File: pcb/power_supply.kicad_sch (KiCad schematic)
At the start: 39 parts, among them J101 TO_IO, U101 10M02SCE144, U102 74LVC2G17, U103 74LVC2G17, U104 74LVC2G17, U105 74LVC2G17

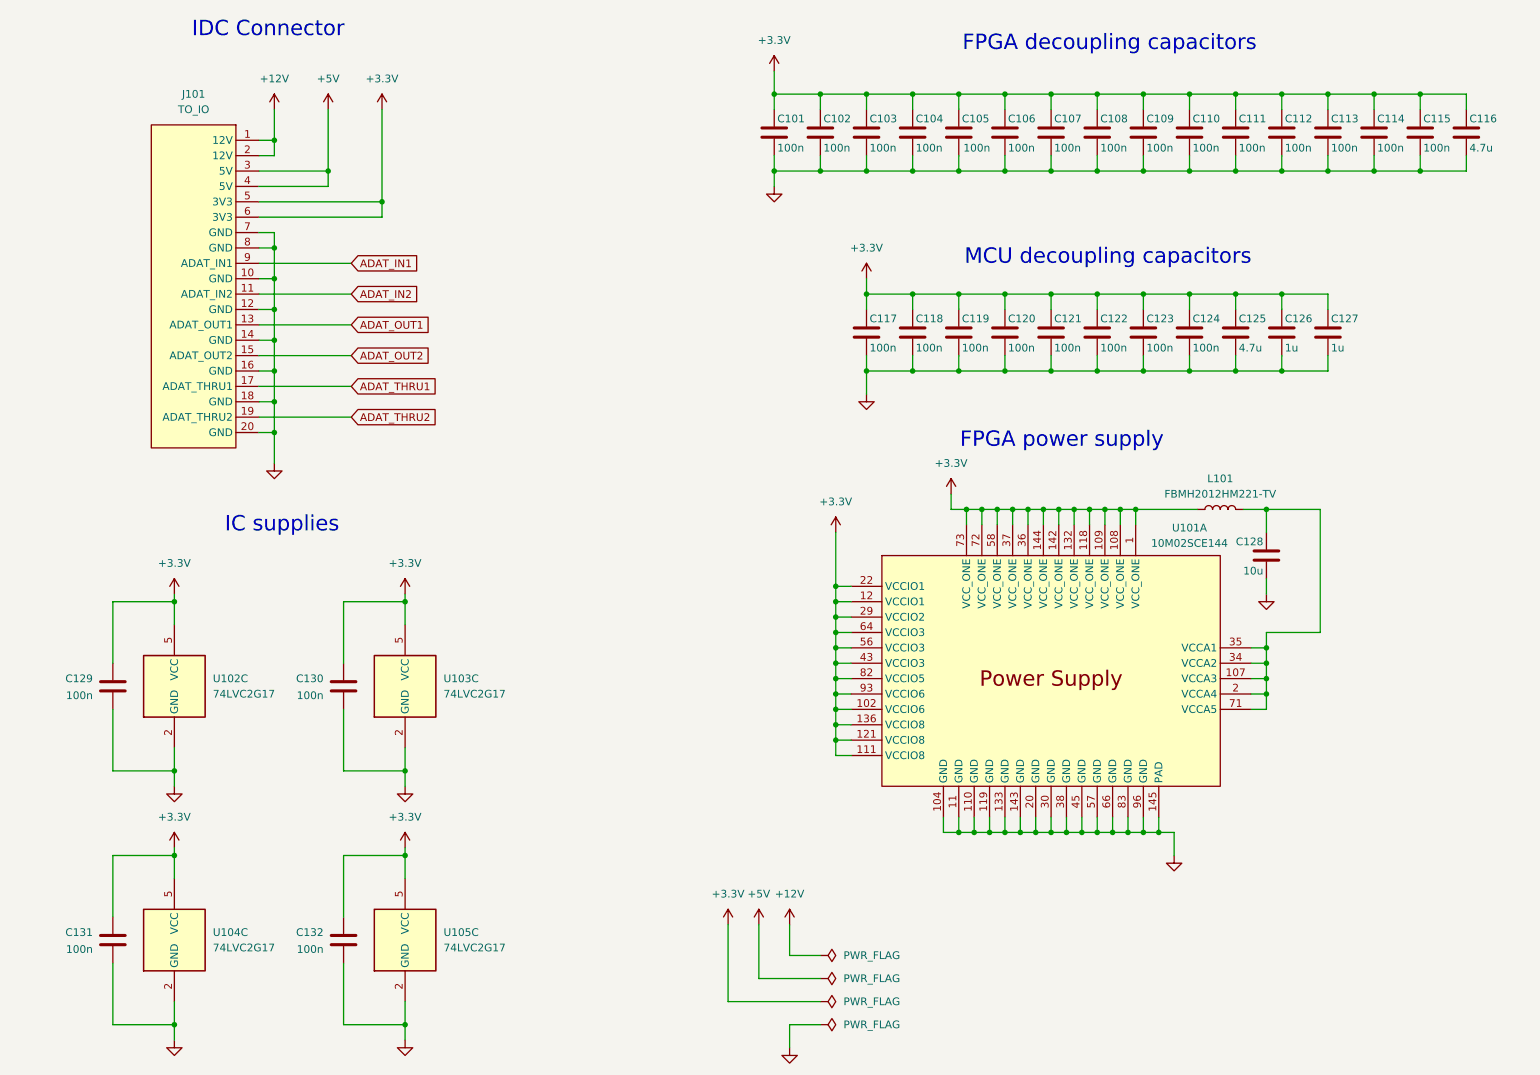
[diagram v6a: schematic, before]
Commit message: Start routing main board
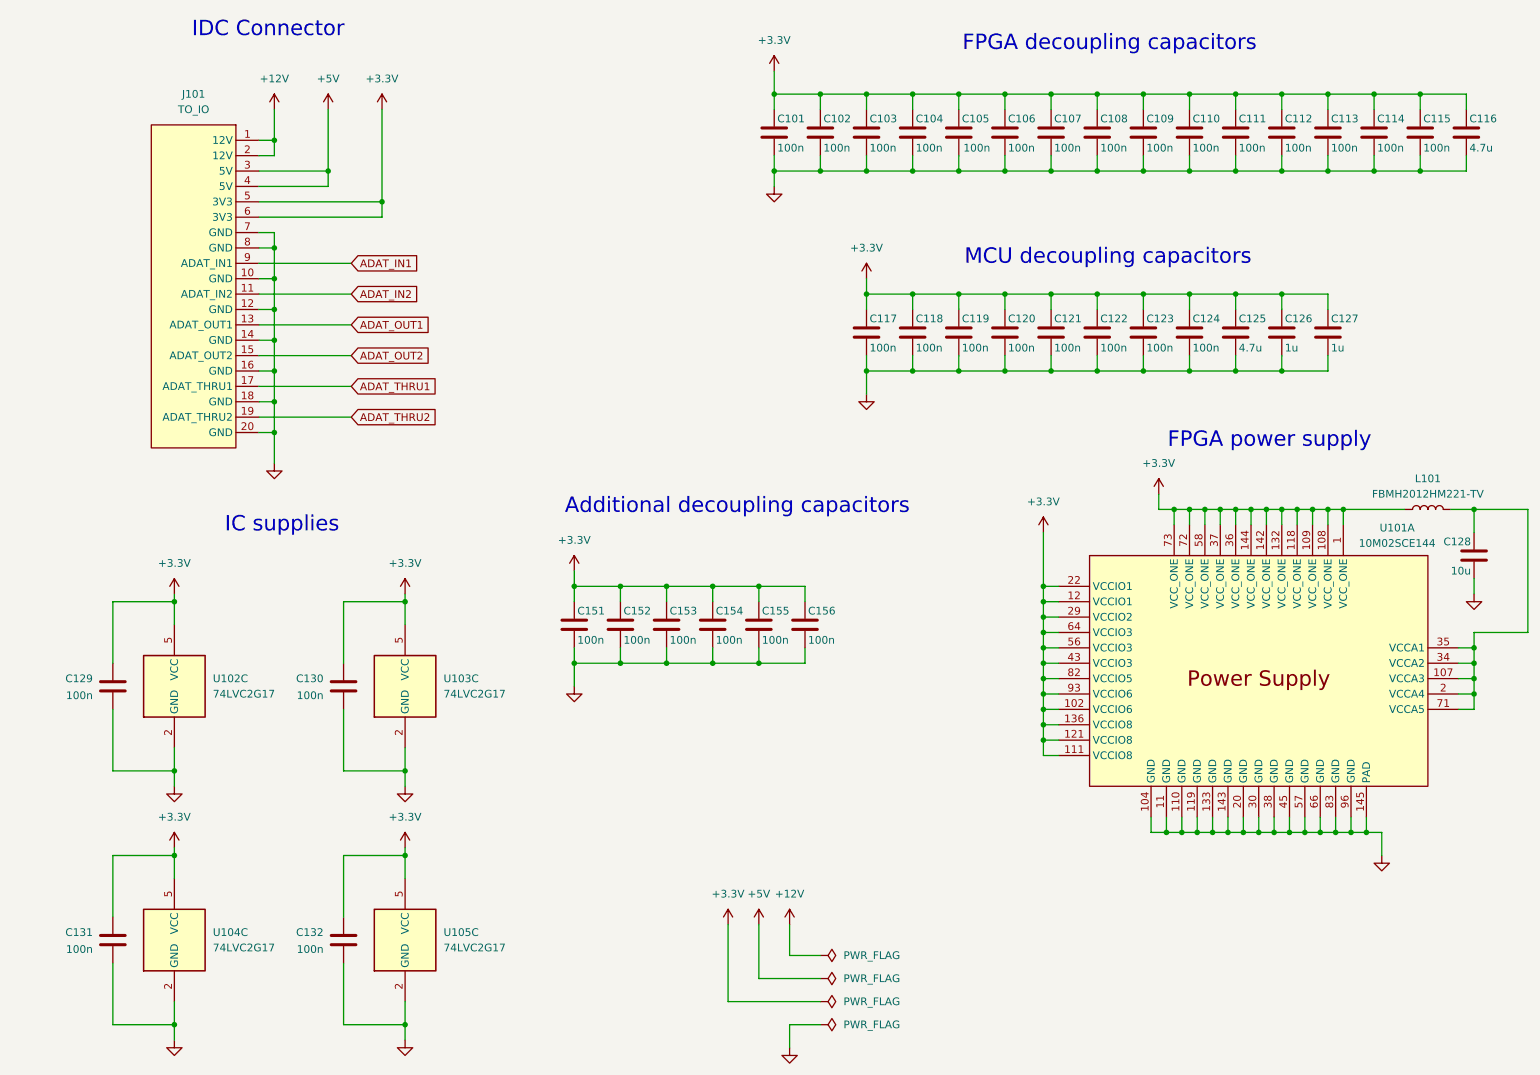
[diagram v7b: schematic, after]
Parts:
- added C151, C152, C153, C154, C155, C156: 100n, Capacitor_SMD:C_0805_2012Metric_Pad1.18x1.45mm_HandSolder, symbol Device:C
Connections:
- net +3.3V: now also C151.1, C152.1, C153.1, C154.1, C155.1, C156.1
- net GND: now also C151.2, C152.2, C153.2, C154.2, C155.2, C156.2
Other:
- note added: "Additional decoupling capacitors"
- moved on the sheet: C128, L101, U101A

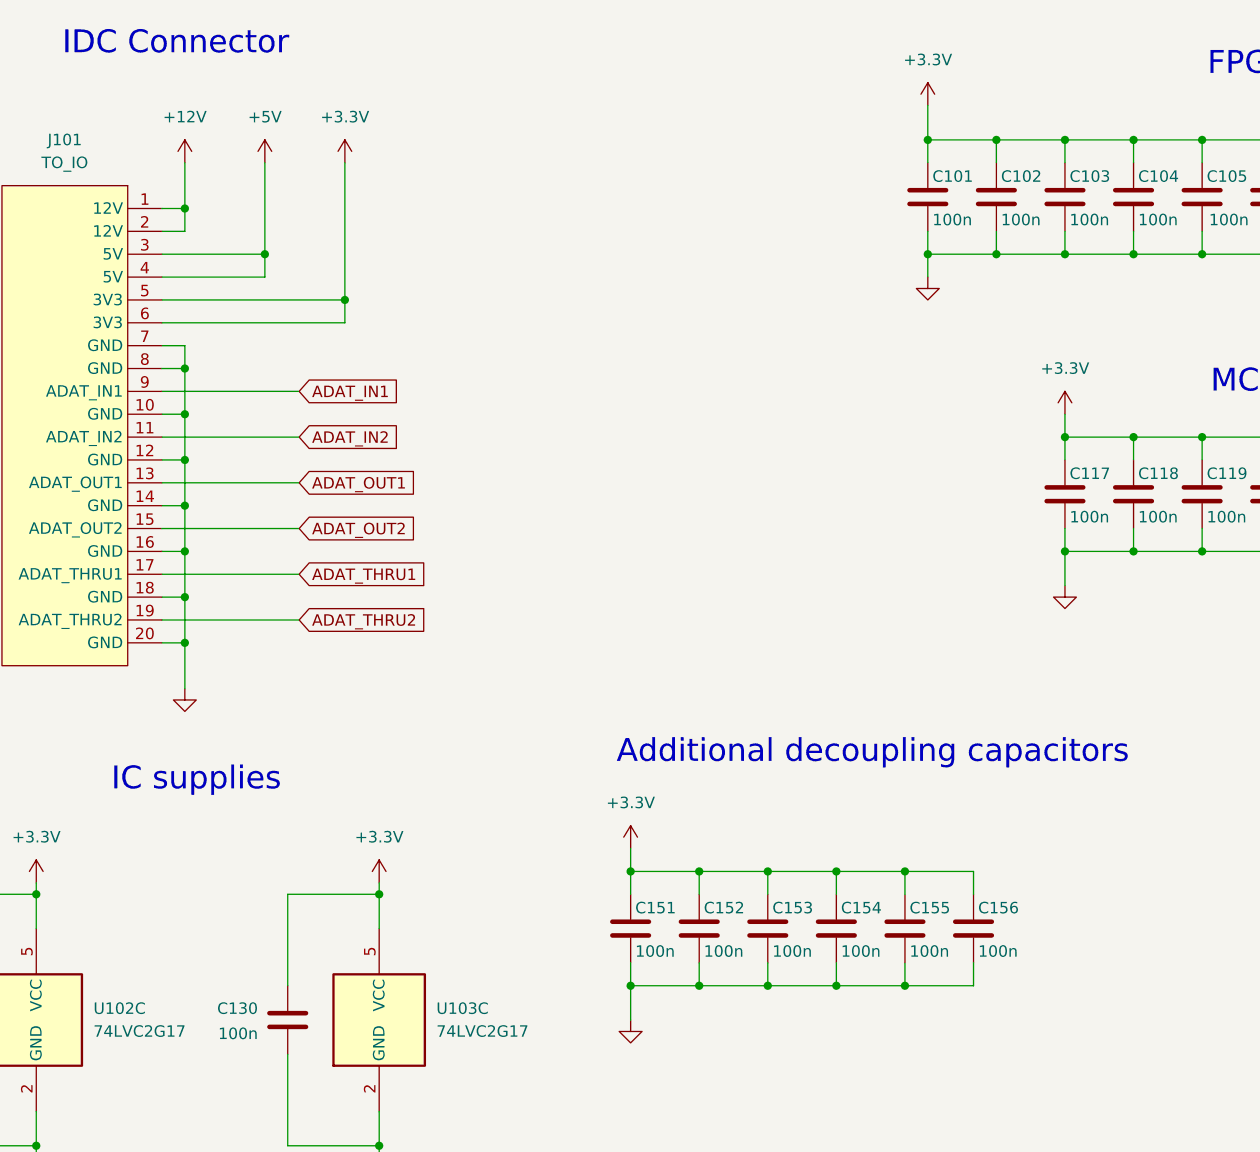
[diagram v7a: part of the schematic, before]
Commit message: Finish first revision of main pcb
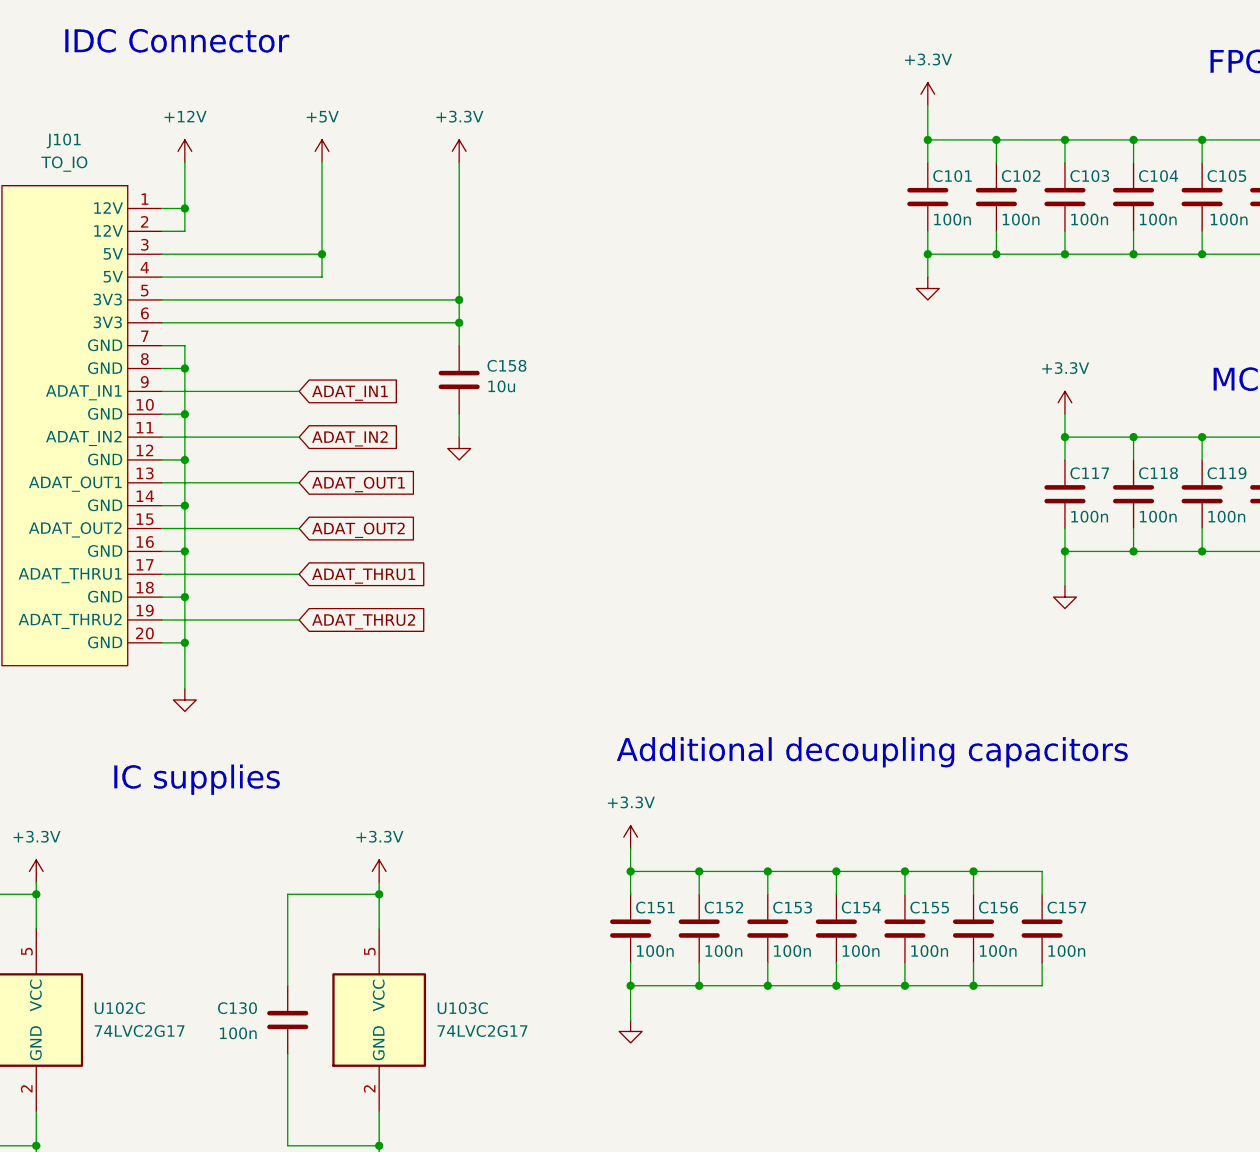
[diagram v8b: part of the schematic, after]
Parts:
- added C157: 100n, Capacitor_SMD:C_0805_2012Metric_Pad1.18x1.45mm_HandSolder, symbol Device:C
- added C158: 10u, Capacitor_SMD:C_1206_3216Metric_Pad1.33x1.80mm_HandSolder, symbol Device:C
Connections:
- net +3.3V: now also C157.1, C158.1
- net GND: now also C157.2, C158.2
